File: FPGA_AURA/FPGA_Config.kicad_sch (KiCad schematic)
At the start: 35 parts, among them U1 XC7A35T-2FTG256C, U2 W25Q256JVEIQ, U3 FT2232HQ, U5 USBLC6-2SC6, U6 93LC56BT-I_SN, Y1 12MHz

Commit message: Added AI-generated todo list, started organising repository, and clear goal defined.
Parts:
- removed C10, C12, C14, C17, C3, C4, C5, C6, C7, C8, C9: 100n, Capacitor_SMD:C_0402_1005Metric, symbol Device:C
- removed C11, C13, C2: 4u7, Capacitor_SMD:C_0402_1005Metric, symbol Device:C
- removed C15, C16: 27pF, Capacitor_SMD:C_0402_1005Metric, symbol Device:C
- removed FB1, FB2: 120R, Inductor_SMD:L_0603_1608Metric, symbol Device:FerriteBead_Small
- removed R2, R3: 22R, Resistor_SMD:R_0402_1005Metric, symbol Device:R
- removed R4: 1k, Resistor_SMD:R_0402_1005Metric, symbol Device:R
- removed R5, R6: 12k, Resistor_SMD:R_0402_1005Metric, symbol Device:R
- removed U3: FT2232HQ, FT2232HQ:QFN50P900X900X100-65N, symbol FT2232HQ:FT2232HQ
- removed U5: USBLC6-2SC6, Package_TO_SOT_SMD:SOT-23-6, symbol Power_Protection:USBLC6-2SC6
- removed U6: 93LC56BT-I_SN, 93LC56BT-I_SN:SOIC127P600X175-8N, symbol 93LC56BT-I_SN:93LC56BT-I_SN
- removed Y1: 12MHz, X322512MSB4SI, symbol X322512MSB4SI:X322512MSB4SI
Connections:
- no-connect marks 30 -> 2
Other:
- moved on the sheet: C1, D107, R1, R110, R111, R7, U1A, U2

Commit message: Connector pinnout defined loosly. Next is schematic clean-up followed by routing.
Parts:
- added D1: LED, LED_SMD:LED_0603_1608Metric, symbol Device:LED
- added R2: 22R, Resistor_SMD:R_0402_1005Metric, symbol Device:R
- added R3: 4k7, Resistor_SMD:R_0402_1005Metric, symbol Device:R
- added R4, R5: 0R, Resistor_SMD:R_0402_1005Metric, symbol Device:R
- added R6: 330R, Resistor_SMD:R_0402_1005Metric, symbol Device:R
- R110: value 200R -> 330R
- R7: value 12k -> 100R
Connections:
- net +3V3: now also R3.2, R4.2, R6.2; no longer R7.1
- net GND: now also D1.1 (K), R5.1; no longer U1.M11 (M2_0)
- net INIT_B_0: now also R6.1
- net TCK: now reaches U1.L7 (TCK_0)
- net PROG_B: now reaches U1.L9 (PROGRAM_B_0)
- net PROG_B: now also R3.1
- net TMS: now reaches U1.M7 (TMS_0)
- net TDI: now reaches U1.N7 (TDI_0)
- net TDO: now reaches U1.N8 (TDO_0)
- net TDO: now also R2.1, R2.2
- new net INIT_LED: D1.2 (A), R7.1
- new net M2_0: R4.1, R5.2, U1.M11 (M2_0)

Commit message: Finished schematic to start routing again, and started MII fanout from connector.
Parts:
- renumbered C1 to C300, D1 to D300, D107 to D301, R3 to R300, R4 to R301, R5 to R302, R2 to R303, R1 to R304, R6 to R305, R7 to R306, R110 to R307, R111 to R308
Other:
- company: (none) -> Alexander Armitage
- title: (none) -> XC7A35T Configuration
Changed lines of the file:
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@@
 	(generator_version "10.0")
 	(paper "A4")
+	(title_block
+		(title "XC7A35T Configuration")
+		(company "Alexander Armitage")
+	)
 	(junction
 		(at 100.33 127)
@@
 		(in_pos_files yes)
 		(dnp no)
-		(property "Reference" "R2"
+		(property "Reference" "R303"
 			(at 97.79 82.55 90)
 			(show_name no)
@@
 			(project "FPGA_AURA"
 				(path "/3d83cb23-9528-4d06-8969-599520e9eb23/4c613221-464e-4cff-8867-bf431546a544"
-					(reference "R2")
+					(reference "R303")
 					(unit 1)
 				)
@@
 		(dnp no)
 		(fields_autoplaced yes)
-		(property "Reference" "D1"
+		(property "Reference" "D300"
 			(at 214.63 67.6274 90)
 			(show_name no)
@@
 			(project "FPGA_AURA"
 				(path "/3d83cb23-9528-4d06-8969-599520e9eb23/4c613221-464e-4cff-8867-bf431546a544"
-					(reference "D1")
+					(reference "D300")
 					(unit 1)
 				)
@@
 		(in_pos_files yes)
 		(dnp no)
-		(property "Reference" "C1"
+		(property "Reference" "C300"
 			(at 225.806 82.55 0)
 			(show_name no)
@@
 			(project "FPGA_AURA"
 				(path "/3d83cb23-9528-4d06-8969-599520e9eb23/4c613221-464e-4cff-8867-bf431546a544"
-					(reference "C1")
+					(reference "C300")
 					(unit 1)
 				)
@@
 		(dnp no)
 		(fields_autoplaced yes)
-		(property "Reference" "R3"
+		(property "Reference" "R300"
 			(at 106.68 100.3299 0)
 			(show_name no)
@@
 			(project "FPGA_AURA"
 				(path "/3d83cb23-9528-4d06-8969-599520e9eb23/4c613221-464e-4cff-8867-bf431546a544"
-					(reference "R3")
+					(reference "R300")
 					(unit 1)
 				)
@@
 		(dnp no)
 		(fields_autoplaced yes)
-		(property "Reference" "R7"
+		(property "Reference" "R306"
 			(at 213.36 55.8799 0)
 			(show_name no)
@@
 			(project "FPGA_AURA"
 				(path "/3d83cb23-9528-4d06-8969-599520e9eb23/4c613221-464e-4cff-8867-bf431546a544"
-					(reference "R7")
+					(reference "R306")
 					(unit 1)
 				)
@@
 		(dnp no)
 		(fields_autoplaced yes)
-		(property "Reference" "D107"
+		(property "Reference" "D301"
 			(at 196.85 141.2874 90)
 			(show_name no)
@@
 			(project "FPGA_AURA"
 				(path "/3d83cb23-9528-4d06-8969-599520e9eb23/4c613221-464e-4cff-8867-bf431546a544"
-					(reference "D107")
+					(reference "D301")
 					(unit 1)
 				)
@@
 		(dnp no)
 		(fields_autoplaced yes)
-		(property "Reference" "R6"
+		(property "Reference" "R305"
 			(at 213.36 45.7199 0)
 			(show_name no)
@@
 			(project "FPGA_AURA"
 				(path "/3d83cb23-9528-4d06-8969-599520e9eb23/4c613221-464e-4cff-8867-bf431546a544"
-					(reference "R6")
+					(reference "R305")
 					(unit 1)
 				)
@@
 		(in_pos_files yes)
 		(dnp no)
-		(property "Reference" "R1"
+		(property "Reference" "R304"
 			(at 177.8 107.95 90)
 			(show_name no)
@@
 			(project "FPGA_AURA"
 				(path "/3d83cb23-9528-4d06-8969-599520e9eb23/4c613221-464e-4cff-8867-bf431546a544"
-					(reference "R1")
+					(reference "R304")
 					(unit 1)
 				)
@@
 		(dnp no)
 		(fields_autoplaced yes)
-		(property "Reference" "R111"
+		(property "Reference" "R308"
 			(at 195.58 129.5399 0)
 			(show_name no)
@@
 			(project "FPGA_AURA"
 				(path "/3d83cb23-9528-4d06-8969-599520e9eb23/4c613221-464e-4cff-8867-bf431546a544"
-					(reference "R111")
+					(reference "R308")
 					(unit 1)
 				)
@@
 		(dnp yes)
 		(fields_autoplaced yes)
-		(property "Reference" "R4"
+		(property "Reference" "R301"
 			(at 102.87 120.6499 0)
 			(show_name no)
@@
 			(project "FPGA_AURA"
 				(path "/3d83cb23-9528-4d06-8969-599520e9eb23/4c613221-464e-4cff-8867-bf431546a544"
-					(reference "R4")
+					(reference "R301")
 					(unit 1)
 				)
@@
 		(dnp no)
 		(fields_autoplaced yes)
-		(property "Reference" "R5"
+		(property "Reference" "R302"
 			(at 102.87 130.8099 0)
 			(show_name no)
@@
 			(project "FPGA_AURA"
 				(path "/3d83cb23-9528-4d06-8969-599520e9eb23/4c613221-464e-4cff-8867-bf431546a544"
-					(reference "R5")
+					(reference "R302")
 					(unit 1)
 				)
@@
 		(dnp no)
 		(fields_autoplaced yes)
-		(property "Reference" "R110"
+		(property "Reference" "R307"
 			(at 195.58 119.3799 0)
 			(show_name no)
@@
 			(project "FPGA_AURA"
 				(path "/3d83cb23-9528-4d06-8969-599520e9eb23/4c613221-464e-4cff-8867-bf431546a544"
-					(reference "R110")
+					(reference "R307")
 					(unit 1)
 				)

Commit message: Power planes done on layers 3 and 4 as well as almost all mezzanine connections made. QSPI and misc left to do.
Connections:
- net TDO: no longer R303.2, U1.N8 (TDO_0)
- new net TDO_R: R303.2, U1.N8 (TDO_0)
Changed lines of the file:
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@@
 		)
 	)
-	(label "TDO"
-		(at 105.41 87.63 0)
+	(label "TDO_R"
+		(at 102.87 87.63 0)
 		(effects
 			(font

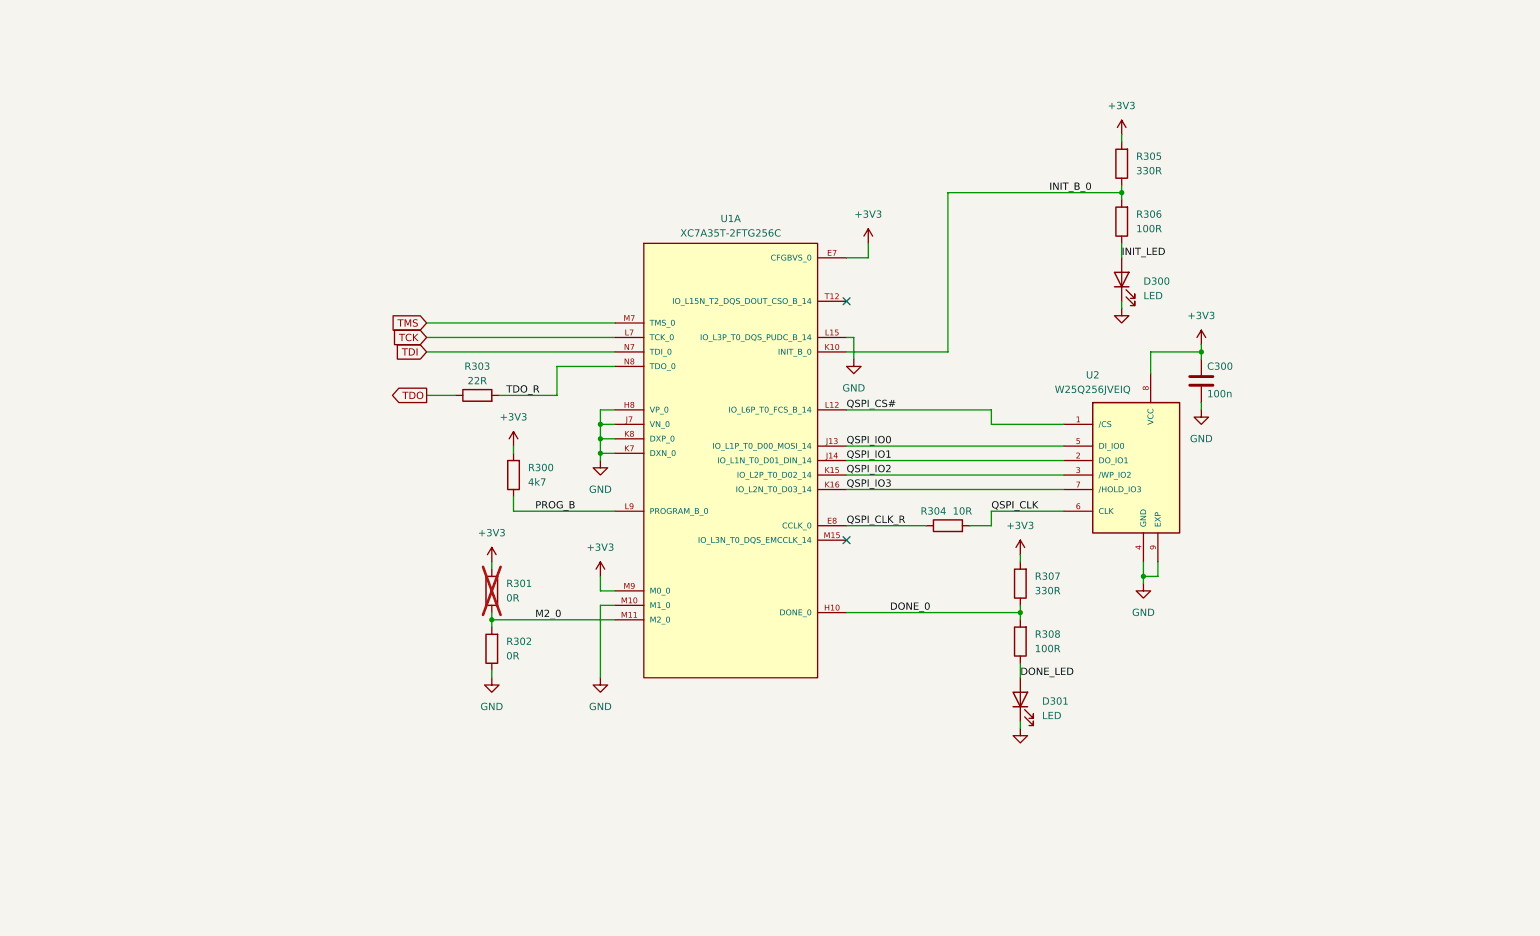
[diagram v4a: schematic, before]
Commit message: Schematic initial draft complete.
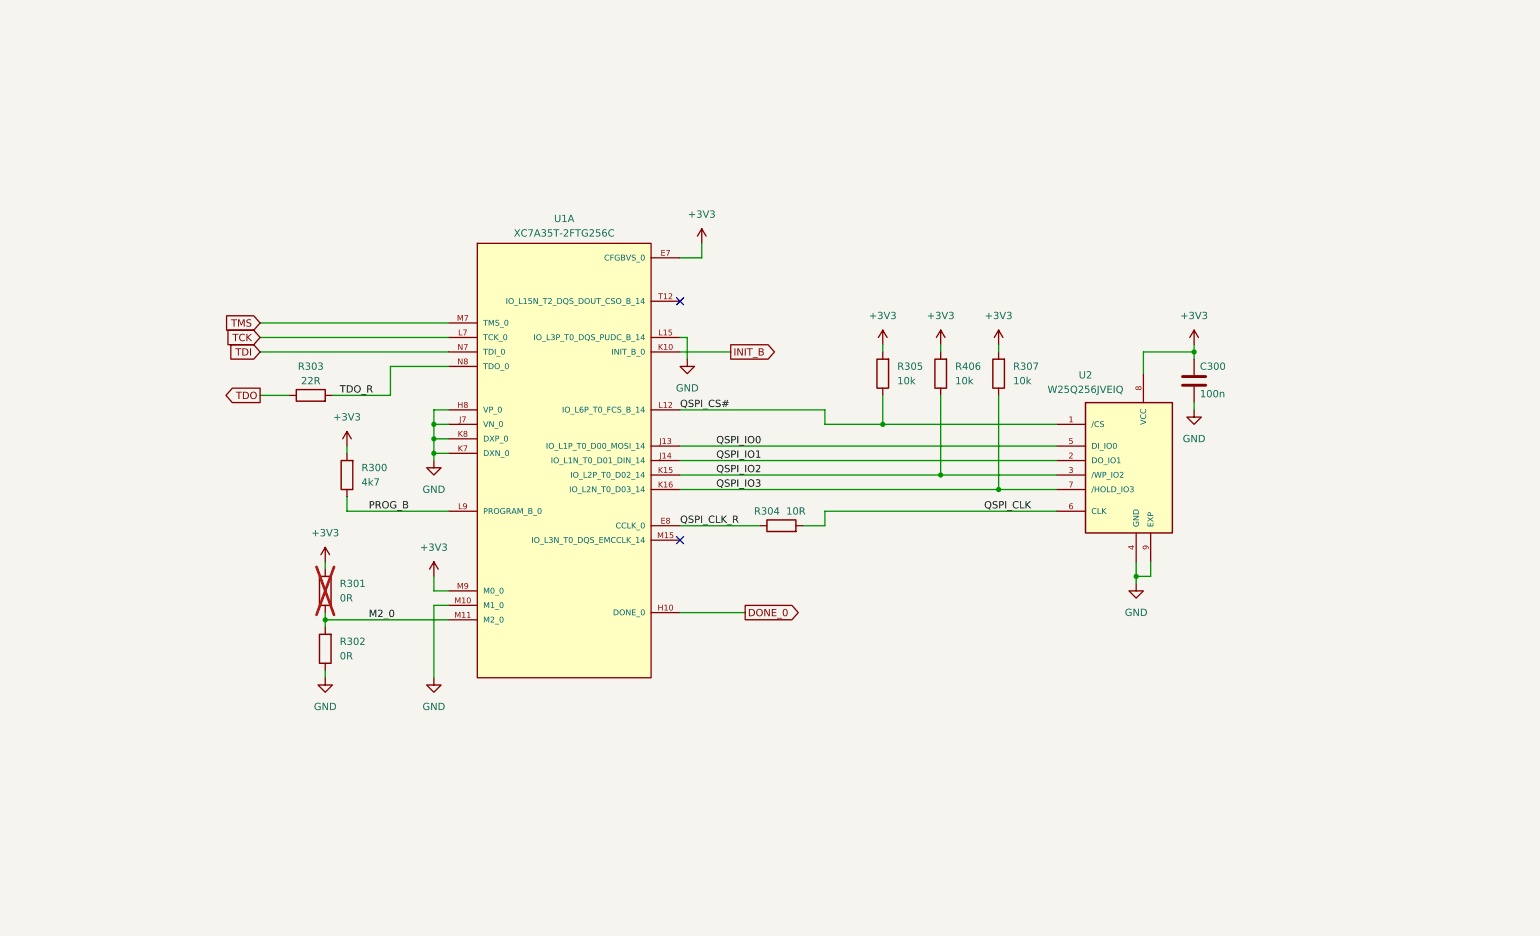
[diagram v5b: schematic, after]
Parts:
- removed D300, D301: LED, LED_SMD:LED_0603_1608Metric, symbol Device:LED
- removed R306, R308: 100R, Resistor_SMD:R_0402_1005Metric, symbol Device:R
- added R406: 10k, Resistor_SMD:R_0402_1005Metric, symbol Device:R
- R305, R307: value 330R -> 10k
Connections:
- net +3V3: now also R406.2
- net DONE_0: no longer R307.1
- net QSPI_CS#: now also R305.1
- net QSPI_IO2: now also R406.1
- net QSPI_IO3: now also R307.1
- net INIT_B_0 renamed INIT_B
- net INIT_B: no longer R305.1
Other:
- moved on the sheet: C300, R300, R301, R302, R303, R304, U1A, U2
